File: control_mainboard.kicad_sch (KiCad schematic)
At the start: 61 parts, among them J201 USB_C_Receptacle_USB2.0_14P, J202 SD_Card_Receptacle, J203 [battery], J204 FFC Connector, J205 SM03B-SRSS-TB, Q201 DMG3415, Q202 DMG3415, SW201 [bootstrap button], SW202 [reset button], SW203 SW_SPST, U201 MCP73831-2-OT, U202 XC6220B331MR, U203 W25Q128JVS, U204 RP2350A, U205 74AHC1G04, U206 W25Q128JVS, Y201 ABM8-272-T3

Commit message: started placing decoupling capacitors
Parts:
- R216: footprint Resistor_SMD:R_0603_1608Metric -> Resistor_SMD:R_0402_1005Metric
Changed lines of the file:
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@@
 			)
 		)
-		(property "Footprint" "Resistor_SMD:R_0603_1608Metric"
+		(property "Footprint" "Resistor_SMD:R_0402_1005Metric"
 			(at 175.26 53.34 0)
 			(hide yes)

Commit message: crystal oscillator
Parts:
- C211, C212: footprint Capacitor_SMD:C_0805_2012Metric -> Capacitor_SMD:C_0402_1005Metric
- R213: footprint Resistor_SMD:R_1206_3216Metric -> Resistor_SMD:R_0402_1005Metric
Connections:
- net at C212.1, Y201.3: now also R213.2; no longer R213.1
- net at U204.22 (XOUT): now also R213.1; no longer R213.2
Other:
- moved on the sheet: R213
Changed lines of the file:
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@@
 			)
 		)
-		(property "Footprint" "Capacitor_SMD:C_0805_2012Metric"
+		(property "Footprint" "Capacitor_SMD:C_0402_1005Metric"
 			(at 148.59 119.38 0)
 			(hide yes)
@@
 			)
 		)
-		(property "Footprint" "Capacitor_SMD:C_0805_2012Metric"
+		(property "Footprint" "Capacitor_SMD:C_0402_1005Metric"
 			(at 148.59 129.54 0)
 			(hide yes)
@@
 	(symbol
 		(lib_id "Device:R_Small")
-		(at 162.56 129.54 90)
+		(at 162.56 129.54 270)
+		(mirror x)
 		(unit 1)
 		(body_style 1)
@@
 			)
 		)
-		(property "Footprint" "Resistor_SMD:R_1206_3216Metric"
+		(property "Footprint" "Resistor_SMD:R_0402_1005Metric"
 			(at 162.56 129.54 0)
 			(hide yes)

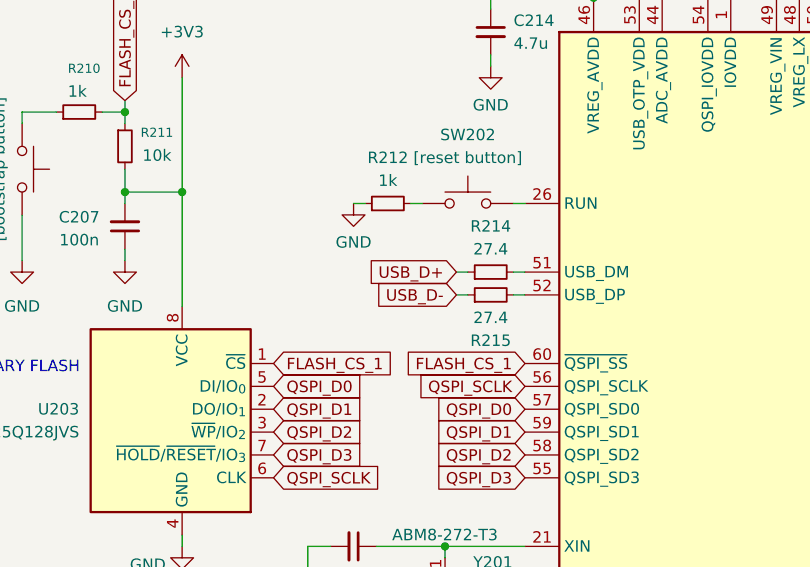
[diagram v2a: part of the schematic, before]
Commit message: flash chip and usb data lines
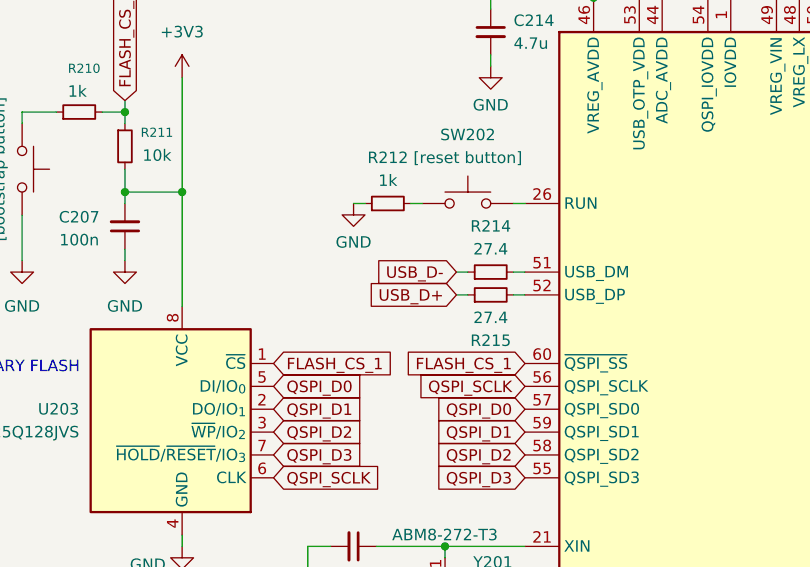
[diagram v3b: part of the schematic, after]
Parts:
- R210, R211: footprint Resistor_SMD:R_1206_3216Metric -> Resistor_SMD:R_0402_1005Metric
- R214, R215: footprint Resistor_SMD:R_0603_1608Metric -> Resistor_SMD:R_0402_1005Metric
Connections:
- net USB_D+: now also R215.1; no longer R214.1
- net USB_D-: now also R214.1; no longer R215.1
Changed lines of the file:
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@@
 	(global_label "USB_D-"
 		(shape input)
-		(at 160.02 91.44 180)
+		(at 160.02 88.9 180)
 		(fields_autoplaced yes)
 		(effects
@@
 		)
 		(property "Intersheetrefs" "${INTERSHEET_REFS}"
-			(at 149.4148 91.44 0)
+			(at 149.4148 88.9 0)
 			(hide yes)
 			(show_name no)
@@
 	(global_label "USB_D+"
 		(shape input)
-		(at 160.02 88.9 180)
+		(at 160.02 91.44 180)
 		(fields_autoplaced yes)
 		(effects
@@
 		)
 		(property "Intersheetrefs" "${INTERSHEET_REFS}"
-			(at 149.4148 88.9 0)
+			(at 149.4148 91.44 0)
 			(hide yes)
 			(show_name no)
@@
 			)
 		)
-		(property "Footprint" "Resistor_SMD:R_1206_3216Metric"
+		(property "Footprint" "Resistor_SMD:R_0402_1005Metric"
 			(at 118.11 71.12 0)
 			(hide yes)
@@
 			)
 		)
-		(property "Footprint" "Resistor_SMD:R_1206_3216Metric"
+		(property "Footprint" "Resistor_SMD:R_0402_1005Metric"
 			(at 123.19 74.93 0)
 			(hide yes)
@@
 			)
 		)
-		(property "Footprint" "Resistor_SMD:R_0603_1608Metric"
+		(property "Footprint" "Resistor_SMD:R_0402_1005Metric"
 			(at 163.83 91.44 0)
 			(hide yes)
@@
 			)
 		)
-		(property "Footprint" "Resistor_SMD:R_0603_1608Metric"
+		(property "Footprint" "Resistor_SMD:R_0402_1005Metric"
 			(at 163.83 88.9 0)
 			(hide yes)

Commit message: secondary flash
optional, don't anticipate needing it but who knows, could be useful
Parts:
- R219: footprint Resistor_SMD:R_1206_3216Metric -> Resistor_SMD:R_0402_1005Metric
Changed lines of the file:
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@@
 			)
 		)
-		(property "Footprint" "Resistor_SMD:R_1206_3216Metric"
+		(property "Footprint" "Resistor_SMD:R_0402_1005Metric"
 			(at 267.97 27.94 0)
 			(hide yes)

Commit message: fixed ground fragmentation
don't break the ground plane under the qspi traces idiot
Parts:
- C203: footprint Capacitor_SMD:C_0805_2012Metric -> Capacitor_SMD:C_0402_1005Metric
- R205, R206: footprint Resistor_SMD:R_0805_2012Metric -> Resistor_SMD:R_0402_1005Metric
- R209: footprint Resistor_SMD:R_1206_3216Metric -> Resistor_SMD:R_0402_1005Metric
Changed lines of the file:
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@@
 			)
 		)
-		(property "Footprint" "Capacitor_SMD:C_0805_2012Metric"
+		(property "Footprint" "Capacitor_SMD:C_0402_1005Metric"
 			(at 74.93 53.34 0)
 			(hide yes)
@@
 			)
 		)
-		(property "Footprint" "Resistor_SMD:R_1206_3216Metric"
+		(property "Footprint" "Resistor_SMD:R_0402_1005Metric"
 			(at 54.61 54.61 0)
 			(hide yes)
@@
 			)
 		)
-		(property "Footprint" "Resistor_SMD:R_0805_2012Metric"
+		(property "Footprint" "Resistor_SMD:R_0402_1005Metric"
 			(at 43.18 38.1 0)
 			(hide yes)
@@
 			)
 		)
-		(property "Footprint" "Resistor_SMD:R_0805_2012Metric"
+		(property "Footprint" "Resistor_SMD:R_0402_1005Metric"
 			(at 43.18 40.64 0)
 			(hide yes)
